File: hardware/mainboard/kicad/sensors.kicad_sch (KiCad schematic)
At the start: 11 parts, among them J12 J_QWIIC, U4 ICM-42688-P, U5 BMP390

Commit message: Kartonaut: Name, Missionsabzeichen, Bestückungsdruck neu, Lötstopp blau
- Projekt heißt Kartonaut (Karton + Astronaut); Flüge werden hochgezählt, Erstflug = Kartonaut 1
- Abzeichen als Polygone in hardware/mainboard/kicad/logo.py, SVGs in docs/brand/
- spacecode/ -> firmware/, Bodenstation-Repo groundcode -> kartonaut-ground (Links, .gitignore)
- gen_pcb.py silk: Bestückungsdruck nur neu setzen, auf der gerouteten Platine; 1,0 mm Schrift,
  freie Plätze statt Überlappungen, Kurznamen an den Steckern, Testpunkte mit Netznamen,
  kleines Abzeichen vorn; hinten Abzeichen 20 mm und Steckerbelegung
- Stackup JLC04161H-7628 mit blauem Lötstopp im Board, Renders mit Stackup-Farben
- DRC-Druckwarnungen 167 -> 14 (Rest aus Footprint-Umrissen)

Co-Authored-By: Claude Opus 5.5 <noreply@anthropic.com>
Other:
- company: Mission Space -> Kartonaut
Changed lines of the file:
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@@
 		(date "2026-10-21")
 		(rev "B")
-		(company "Mission Space")
+		(company "Kartonaut")
 		(comment 1 "IMU ICM-42688-P an SPI1, Barometer BMP390 und Qwiic an I2C")
 		(comment 2 "erzeugt aus circuit.py (gen_schematic.py)")

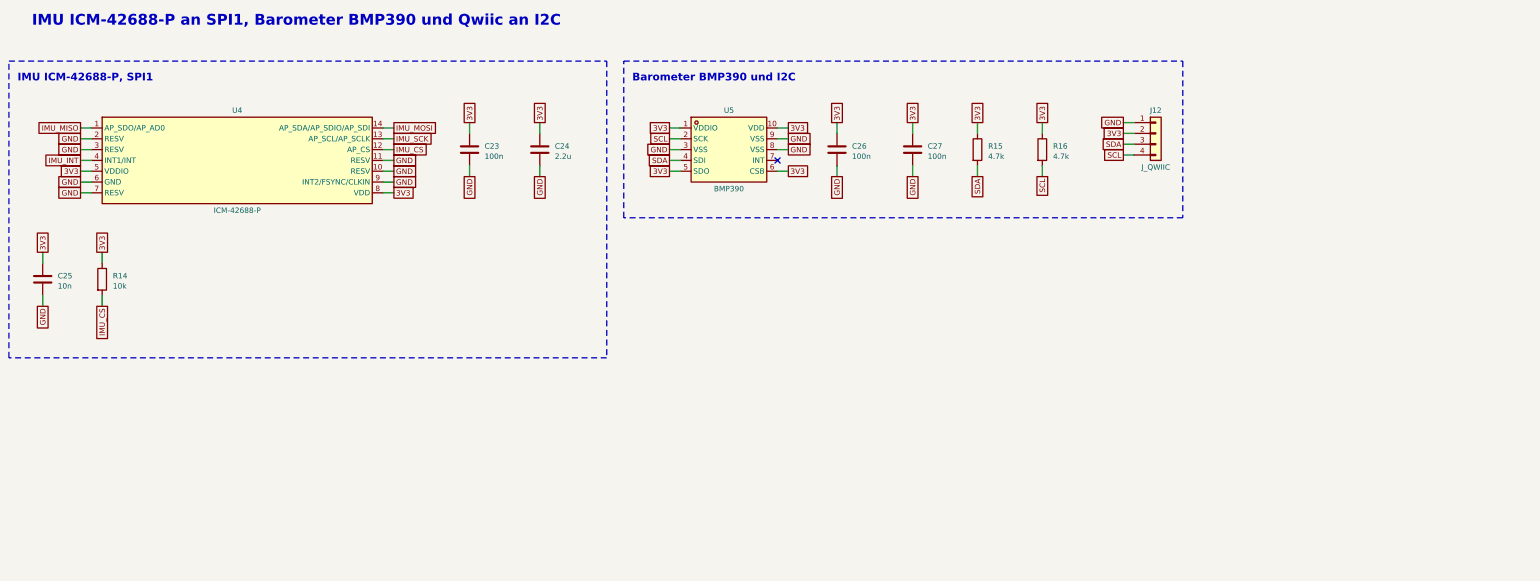
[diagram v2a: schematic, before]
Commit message: Mainboard rev B1: Review A1-A8 und Entscheidungen E1-E10 eingearbeitet, 2S-Pfad als F.Cu-Flaechen, 28 Verbindungen offen
Schaltung (circuit.py, ERC 0, Netzliste gegen README §4 OK): Hold-up hinter D1, EN-Teiler 330k/115k,
P-FET-Lastschalter je Akku, Polyfuse je Akku, Kelvin-Shunt mit INA239 an SPI1, BMP390 an SPI1,
74HC138/74HC4051 mit gemeinsamer Adresse, J_STACK 2x10 mit LDO 3V3_EXP, 1S-Lader MCP73831,
J_CHG2, vier Pyro-Kanaele (3/4 DNP), vierter Servo, alle Servos und Rollmotor an VSERVO,
3V3_SENS, eine WS2812B-Kette, Summer Pin 37, E22 NRST Pin 6; 166 Bauteile.

Platine (gen_pcb.py): neue Platzierung, 2S-Pfad, Pyro-Ausgaenge und VSYS_IN als F.Cu-Flaechen mit
Sperrflaechen fuer Freerouting, Strom-Klasse nur F.Cu, IMU-Zone 5 mm, patch mit Umweg ueber In2.
DRC 0 Fehler, Paritaet 0, kein 2S-Netz auf In2; 28 offene Verbindungen, Liste in kicad/README.md §5.5.
Spezifikation README.md und kicad/README.md auf B1 nachgezogen, review_check_layout.py fuer B1.

Co-Authored-By: Claude Opus 5.5 <noreply@anthropic.com>
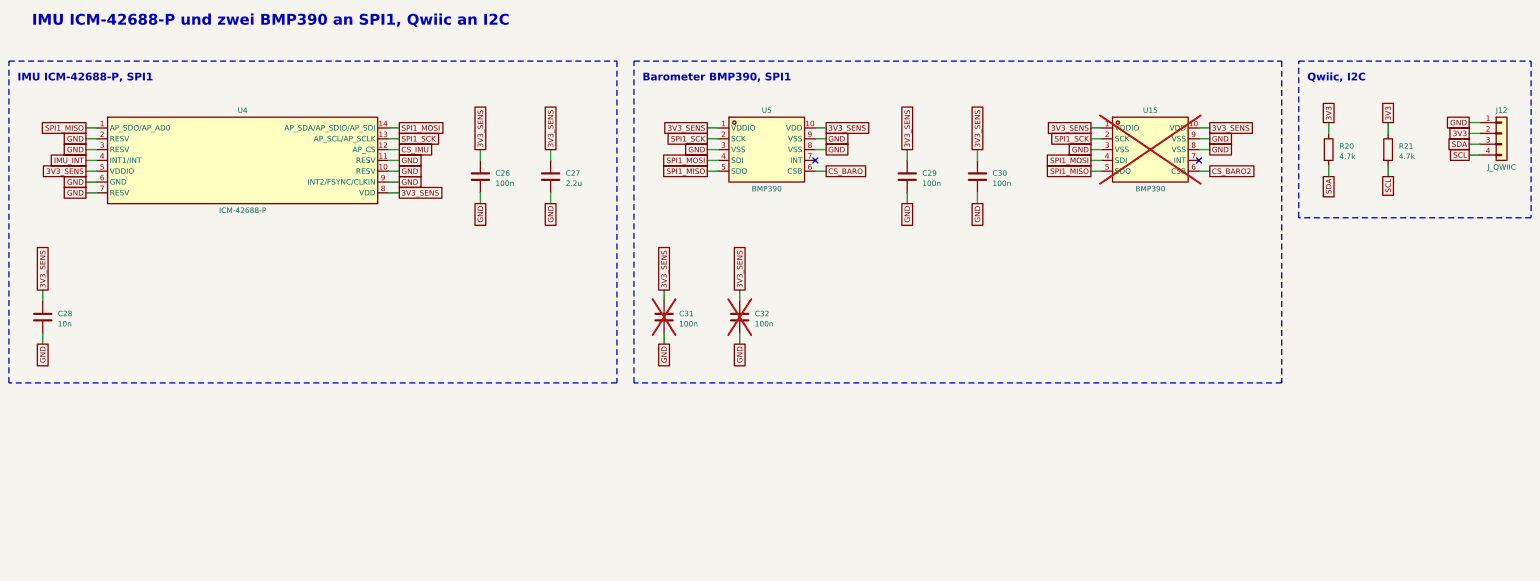
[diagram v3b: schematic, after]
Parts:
- removed C23: 100n, Capacitor_SMD:C_0603_1608Metric, symbol Device:C
- removed C24: 2.2u, Capacitor_SMD:C_0603_1608Metric, symbol Device:C
- removed C25: 10n, Capacitor_SMD:C_0603_1608Metric, symbol Device:C
- removed R14: 10k, Resistor_SMD:R_0603_1608Metric, symbol Device:R
- removed R15, R16: 4.7k, Resistor_SMD:R_0603_1608Metric, symbol Device:R
- added C28: 10n, Capacitor_SMD:C_0603_1608Metric, symbol Device:C
- added C29, C30, C31, C32: 100n, Capacitor_SMD:C_0603_1608Metric, symbol Device:C
- added R20, R21: 4.7k, Resistor_SMD:R_0603_1608Metric, symbol Device:R
- added U15: BMP390, lcsc:LGA-10_L2.0-W2.0-P0.50-BL, symbol lcsc:BMP390_C5124834
- C27: value 100n -> 2.2u
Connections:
- net 3V3: now also R20.1, R21.1; no longer C26.1, C27.1, U4.5 (VDDIO), U4.8 (VDD), U5.1 (VDDIO), U5.10 (VDD), U5.5 (SDO), U5.6 (CSB)
- net GND: now also C28.2, C29.2, C30.2, C31.2, C32.2, U15.3 (VSS), U15.8 (VSS), U15.9 (VSS)
- net SCL: now also R21.2; no longer U5.2 (SCK)
- net SDA: now also R20.2; no longer U5.4 (SDI)
- net IMU_CS renamed CS_IMU
- net IMU_MISO renamed SPI1_MISO
- net SPI1_MISO: now also U5.5 (SDO), U15.5 (SDO)
- net IMU_MOSI renamed SPI1_MOSI
- net SPI1_MOSI: now also U5.4 (SDI), U15.4 (SDI)
- net IMU_SCK renamed SPI1_SCK
- net SPI1_SCK: now also U5.2 (SCK), U15.2 (SCK)
- new net 3V3_SENS: C26.1, C27.1, C28.1, C29.1, C30.1, C31.1, C32.1, U15.1 (VDDIO), U15.10 (VDD), U4.5 (VDDIO), U4.8 (VDD), U5.1 (VDDIO), U5.10 (VDD)
- new net CS_BARO: U5.6 (CSB)
- new net CS_BARO2: U15.6 (CSB)
- no-connect marks 1 -> 2
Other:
- note added: "Barometer BMP390, SPI1"
- note added: "IMU ICM-42688-P und zwei BMP390 an SPI1, Qwiic an I2C"
- note added: "Qwiic, I2C"
- note removed: "Barometer BMP390 und I2C"
- note removed: "IMU ICM-42688-P an SPI1, Barometer BMP390 und Qwiic an I2C"
- moved on the sheet: C26, C27, J12, U4, U5

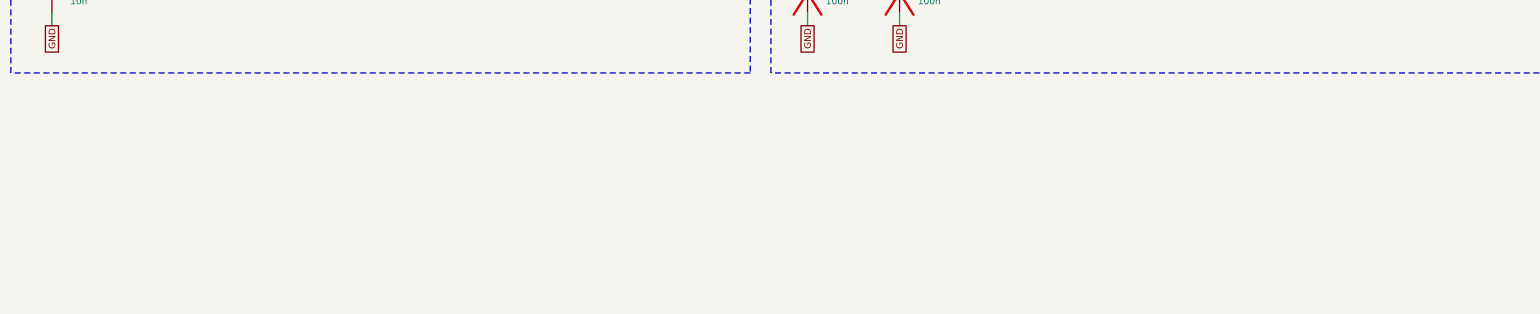
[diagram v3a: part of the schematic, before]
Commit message: Platine rev B1: Magnetometer LIS3MDL und SHT40 bestückt, ADXL375 als DNP-Footprint, alle an I2C und 3V3
Zukunftsfähigkeit (Jan, 23.10.): LIS3MDL (C478483, 0x1E) in der linken Spitzenecke, SHT40 (C2848306, 0x44)
neben J_QWIIC, ADXL375 (C579466, 0x53, DNP) hinter dem USB-Ende des Teensy. I2C statt SPI1, weil die
Spitze nur über das I2C-Paar erreichbar ist und SPI1 der Flugbus bleibt; 3V3 statt 3V3_SENS (45 mm).
Pinbelegungen gegen die Datenblätter geprüft (LIS3MDL Reserved an GND, C1 100 nF; SHT40 Die-Pad frei).

add_parts.py setzt neue Teile aus circuit.py in die fertige Platine (Netze, Blattpfad, DNP, Kupfer unter
den Pads weg); route_gaps.py kann Masse-Vias in Inseln setzen (GND-Inseln, `drop REF-PIN`). ERC 0/0,
Netzlistenprüfung OK, DRC 0 Fehler / 0 offen, Parität 0, Prüfskript ohne Befund; Druck, Renders,
Bestelldateien (132 SMD-Teile, 53 BOM-Zeilen) neu; README, ORDER.md §3.3 und Review-Brief nachgezogen.

Co-Authored-By: Claude Fable 5.1 <noreply@anthropic.com>
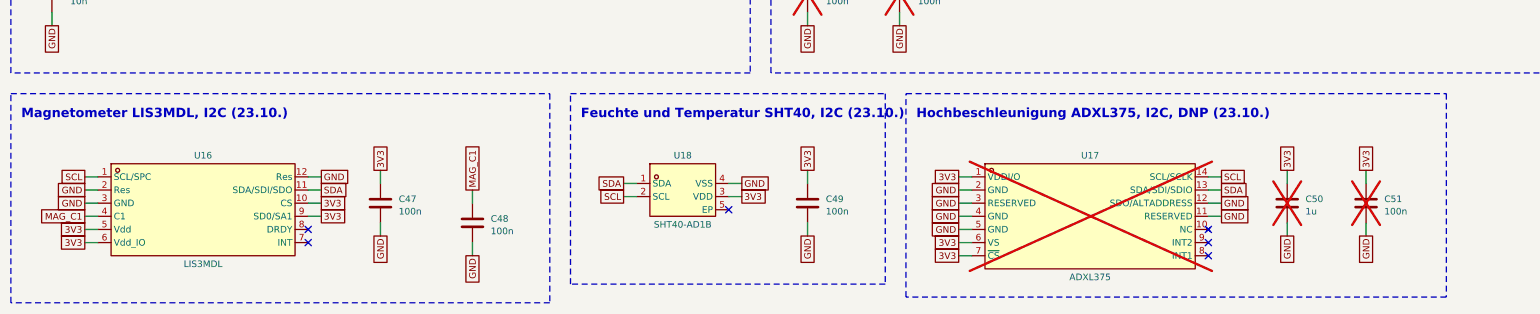
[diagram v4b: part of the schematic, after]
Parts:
- added C47, C48, C49, C51: 100n, Capacitor_SMD:C_0603_1608Metric, symbol Device:C
- added C50: 1u, Capacitor_SMD:C_0603_1608Metric, symbol Device:C
- added U16: LIS3MDL, lcsc:LGA-12_L2.0-W2.0-P0.50-BL, symbol lcsc:LIS3MDLTR
- added U17: ADXL375, lcsc:LGA-14_L5.0-W3.0-P0.80-BL-1, symbol lcsc:ADXL375BCCZ
- added U18: SHT40-AD1B, lcsc:DFN-4_L1.5-W1.5-P0.8-TL-EP, symbol lcsc:SHT40-AD1B-R3
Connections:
- net 3V3: now also C47.1, C49.1, C50.1, C51.1, U16.10 (CS), U16.5 (Vdd), U16.6 (Vdd_IO), U16.9 (SD0/SA1), U17.1 (VDDI/O), U17.6 (VS), U17.7 (~{CS}), U18.3 (VDD)
- net GND: now also C47.2, C48.2, C49.2, C50.2, C51.2, U16.12 (Res), U16.2 (Res), U16.3 (GND), U17.11 (RESERVED), U17.12 (SDO/ALTADDRESS), U17.2 (GND), U17.3 (RESERVED), U17.4 (GND), U17.5 (GND), U18.4 (VSS)
- net SCL: now also U16.1 (SCL/SPC), U17.14 (SCL/SCLK), U18.2 (SCL)
- net SDA: now also U16.11 (SDA/SDI/SDO), U17.13 (SDA/SDI/SDIO), U18.1 (SDA)
- new net MAG_C1: C48.1, U16.4 (C1)
- no-connect marks 2 -> 8
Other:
- note added: "Feuchte und Temperatur SHT40, I2C (23.10.)"
- note added: "Hochbeschleunigung ADXL375, I2C, DNP (23.10.)"
- note added: "Magnetometer LIS3MDL, I2C (23.10.)"

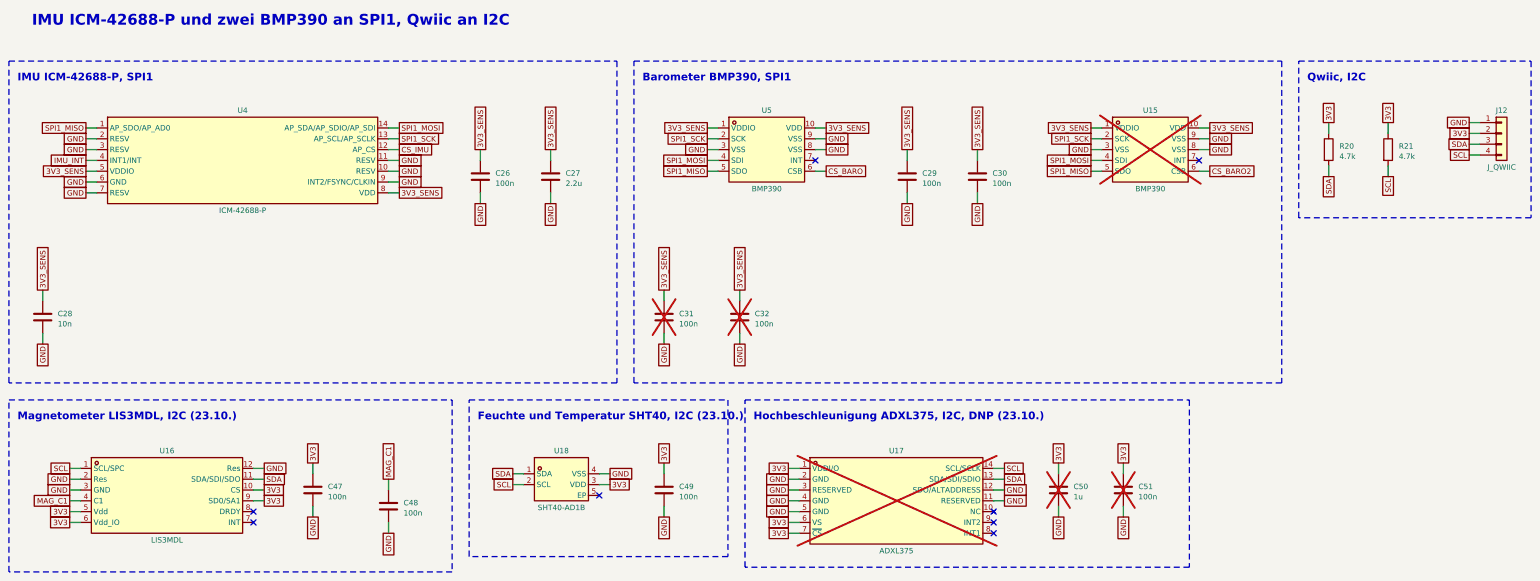
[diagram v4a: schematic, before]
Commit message: Platine rev B1: SPI0 auf J_STACK (E11), IMU LSM6DSV16X statt ICM-42688-P (E12), DRC 0/0
- J_STACK Pin 7/8/9 an SPI0 (Teensy 13/11/12) statt SPI1; nSLEEP -> 40, PYRO3_FIRE -> 41,
  PWM_EXT -> 33, LORA_M0 -> 16; keine Reservepins mehr (circuit.py, check_design.py, Doku)
- IMU LSM6DSV16X (C5267406) auf dem LGA-14-Footprint des ICM: Pins 2/3 an GND, 9-11 offen
  (AN5763 Tab. 1), JLC-Preis 3,4 statt 21,5 USD; Massepfad der IMU-Pads 2/3/6/7 ueber C26,
  3V3_SENS von Pad 5 ueber C26/C28 zu Pad 8
- die sieben neuen Wege von Hand geplant (eigene Sitzung 24.10.): 59 Vias, 13 kurze Stuecke
  auf B.Cu; SPI0_MISO 114 mm, SPI0-Takt zur Zusatzplatine hoechstens 8 MHz
- Reststummel (PYRO1_SENSE, PYRO4_SENSE, CS_IMU-Via, doppeltes GND-Via) entfernt
- sync_fields.py: Bauteilfelder der Platine aus circuit.py (Paritaet 0 ohne Neuerzeugung)
- DRC 0 Fehler, 0 offen, Paritaet 0; Pruefskript ohne Befund; Bestelldateien und Bilder neu
- Doku: Spezifikation, ORDER.md, Review-Brief, kicad-README (Par. 5.5 Tabelle der Wege, Par. 6
  E11/E12), Komponenten, Root-READMEs, PROJECT.md; HANDROUTING_SPI0.md

Co-Authored-By: Claude Fable 5.1 <noreply@anthropic.com>
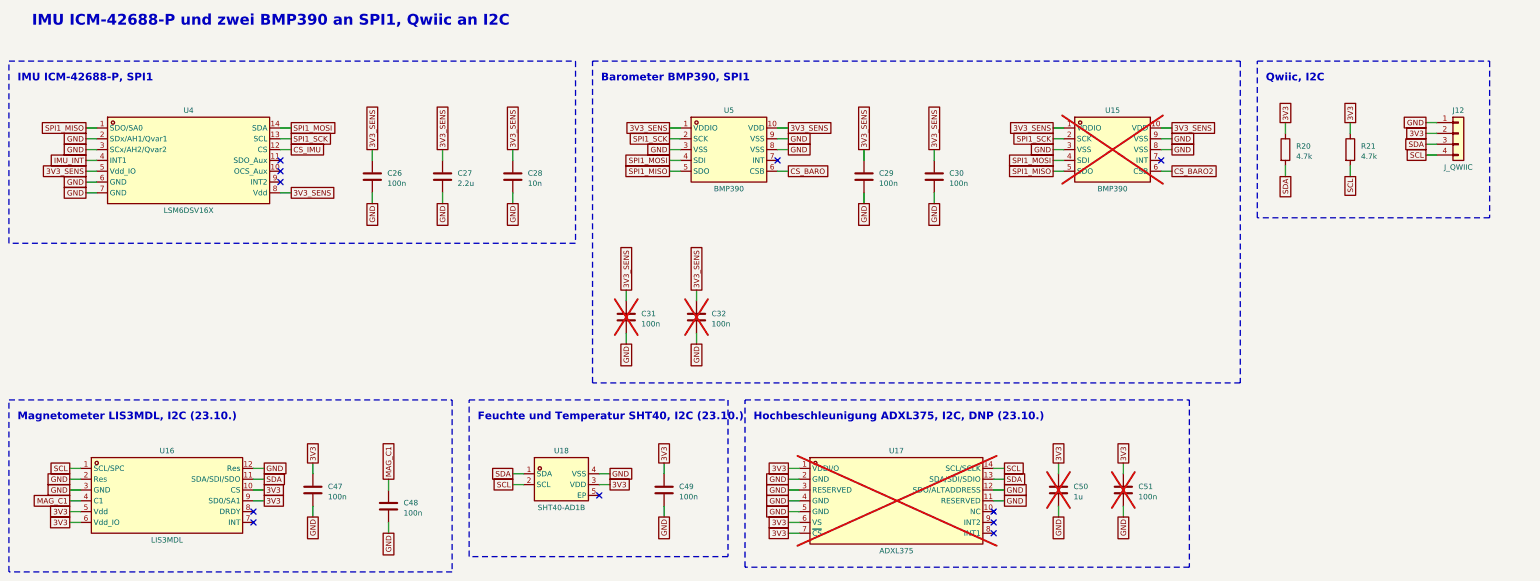
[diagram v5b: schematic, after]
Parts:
- U4: value ICM-42688-P -> LSM6DSV16X; symbol lcsc:ICM-42688-P -> lcsc:LSM6DSV16XTR; LCSC C1850418 -> C5267406
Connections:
- net GND: no longer U4.10 (RESV), U4.11 (RESV), U4.9 (INT2/FSYNC/CLKIN)
- no-connect marks 8 -> 11
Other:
- moved on the sheet: C26, C27, C28, C29, C30, C31, C32, J12, R20, R21, U15, U5

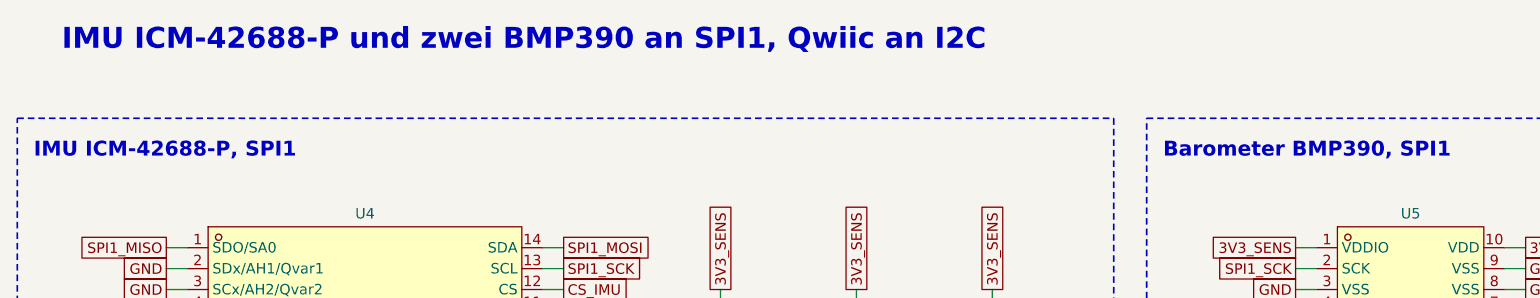
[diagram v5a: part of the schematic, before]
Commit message: Mainboard rev B1: Prüfanleitung für das Review und Einkaufsliste (alles außer JLCPCB); Blatt Sensorik: Titel auf LSM6DSV16X
Co-Authored-By: Claude Fable 5.1 <noreply@anthropic.com>
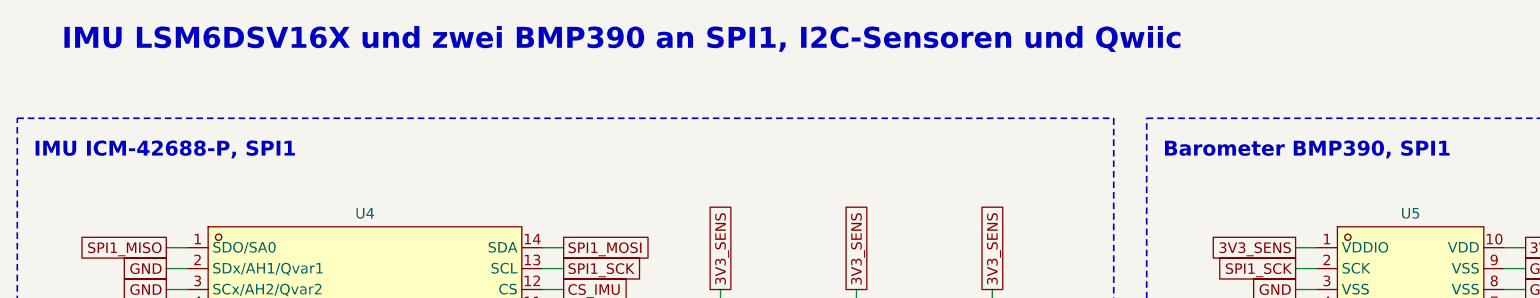
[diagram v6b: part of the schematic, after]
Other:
- note added: "IMU LSM6DSV16X und zwei BMP390 an SPI1, I2C-Sensoren und Qwiic"
- note removed: "IMU ICM-42688-P und zwei BMP390 an SPI1, Qwiic an I2C"
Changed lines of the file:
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@@
 		(rev "B")
 		(company "Kartonaut")
-		(comment 1 "IMU ICM-42688-P und zwei BMP390 an SPI1, Qwiic an I2C")
+		(comment 1 "IMU LSM6DSV16X und zwei BMP390 an SPI1, I2C-Sensoren und Qwiic")
 		(comment 2 "erzeugt aus circuit.py (gen_schematic.py)")
 	)
-	(text "IMU ICM-42688-P und zwei BMP390 an SPI1, Qwiic an I2C"
+	(text "IMU LSM6DSV16X und zwei BMP390 an SPI1, I2C-Sensoren und Qwiic"
 		(exclude_from_sim no)
 		(at 25.4 22 0)
